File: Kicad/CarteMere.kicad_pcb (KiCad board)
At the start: 4 copper layers, 91 x 95 mm, 120 parts, among them J1 Conn_01x06, J10 Conn_01x04, J12 Conn_01x06, J13 Conn_01x06, J14 Conn_01x04, J15 Conn_01x04, J16 Conn_01x04, J18 Conn_01x06, J19 Conn_01x06, J2 Conn_01x10, J21 Conn_01x04, J22 Conn_01x04, J23 Conn_01x04, J24 Conn_01x02, J25 Conn_01x06, J26 Conn_01x02, J27 Conn_01x06, J28 Conn_01x06, J29 Conn_01x06, J3 Conn_01x10, J30 Conn_01x06, J31 Conn_01x02, J32 Conn_01x09, J33 Conn_01x05, J34 Conn_01x05, J35 Conn_01x05, J36 Conn_01x05, J37 Conn_01x05, J39 Conn_01x09, J4 Conn_01x10, J40 Conn_01x09, J41 Conn_01x05, J42 Conn_01x05, J43 Conn_01x05, J44 Conn_01x05, J45 Conn_01x05, J46 Conn_01x05, J47 Conn_01x05, J48 USB_C_Receptacle_USB2.0_16P, J49 Conn_01x02, J5 Conn_01x06, J50 Conn_ST_STDC14, J6 Conn_01x06, J7 Conn_01x06, J8 Conn_01x04, J9 Conn_01x04, SW1 SW_MEC_5E, U2 USBLC6-2P6, U3 STM32H573IITxQ

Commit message: ajout spi et maj readme
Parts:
- removed J15, J21, J23: Conn_01x04, Connector_PinHeader_2.54mm:PinHeader_1x04_P2.54mm_Vertical
- removed J24, J26, J31: Conn_01x02, Connector_PinHeader_2.54mm:PinHeader_1x02_P2.54mm_Vertical
- removed J4: Conn_01x10, Connector_PinHeader_2.54mm:PinHeader_1x10_P2.54mm_Vertical
- added J11: Conn_01x07, Connector_JST:JST_EH_B7B-EH-A_1x07_P2.50mm_Vertical, F.Cu at (161.5, 101.1)
- added J17: Conn_01x07, Connector_JST:JST_EH_B7B-EH-A_1x07_P2.50mm_Vertical, F.Cu at (167.7, 101.1)
- added R23: 51, Resistor_SMD:R_0402_1005Metric, B.Cu at (143.2, 78.5)
- J10: value Conn_01x04 -> Conn_01x05; footprint Connector_PinHeader_2.54mm:PinHeader_1x04_P2.54mm_Vertical -> Connector_JST:JST_EH_B5B-EH-A_1x05_P2.50mm_Vertical
- J16: value Conn_01x04 -> Conn_01x07; footprint Connector_PinHeader_2.54mm:PinHeader_1x04_P2.54mm_Vertical -> Connector_JST:JST_EH_B7B-EH-A_1x07_P2.50mm_Vertical
- J2, J3: value Conn_01x10 -> Conn_01x07; footprint Connector_PinHeader_2.54mm:PinHeader_1x10_P2.54mm_Vertical -> Connector_PinHeader_2.54mm:PinHeader_1x07_P2.54mm_Vertical
- J8: value Conn_01x04 -> Conn_01x07; footprint Connector_PinHeader_2.54mm:PinHeader_1x04_P2.54mm_Vertical -> Connector_PinHeader_2.54mm:PinHeader_1x07_P2.54mm_Vertical
- JP1: footprint TestPoint:TestPoint_2Pads_Pitch2.54mm_Drill0.8mm -> Connector_PinHeader_2.54mm:PinHeader_1x02_P2.54mm_Vertical
- SW1: footprint BoutonSMD:wurth_pushButton_SMD -> Switch:WS-TASU SMT Tact Switch 4.7x3.5 mm side push
- moved SW1 85.4 mm to (107.2, 142.7)
- moved J10 79.1 mm to (173.7, 89.3), turned to -90 degrees
- moved C6 77.0 mm to (108.9, 139.5), turned to 0 degrees
- moved J16 56.9 mm to (120.1, 78.8)
- moved J8 45.1 mm to (116.9, 103.8), turned to 180 degrees
- moved R14 17.7 mm to (157.6, 95.7)
- moved J37 6.97 mm to (105.1, 102.8)
- moved C34 6.50 mm to (160.9, 90.0)
- moved C35 6.50 mm to (160.9, 93.4)
- moved U4 6.50 mm to (164.8, 91.8)
- moved J34 5.79 mm to (105.1, 85.2)
- moved J2 4.76 mm to (114.4, 103.8)
- moved J3 4.76 mm to (111.8, 103.8)
- moved J42 4.61 mm to (104.1, 118.8)
- moved J44 4.10 mm to (104.1, 125.1)
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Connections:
- J10 pad 1: /TIM8_CH3 -> +3.3V
- J10 pad 2: /TIM8_CH2 -> GND
- J10 pad 3: /TIM8_CH1 -> /UART9_TX
- J10 pad 4: /TIM8_CH4 -> GND
- J16 pad 1: +3.3V -> /GPIO_PB11
- J16 pad 2: +3.3V -> /GPIO_PB10
- J16 pad 3: +3.3V -> /SPI5_SCK
- J16 pad 4: +3.3V -> /SPI5_MOSI
- J18 pad 1: /GPIO_PG0 -> /GPIO_PF14
- J18 pad 2: /GPIO_PG1 -> /GPIO_PF15
- J2 pad 1: /GPIO_PI9 -> +3.3V
- J2 pad 2: /GPIO_PI10 -> +3.3V
- J2 pad 3: /GPIO_PI11 -> +3.3V
- J2 pad 4: /GPIO_PG7 -> +3.3V
- J2 pad 5: /GPIO_PG6 -> +3.3V
- J2 pad 6: /GPIO_PG5 -> +3.3V
- J2 pad 7: /GPIO_PG4 -> +3.3V
- J3 pad 1: +3.3V -> GND
- J3 pad 2: +3.3V -> GND
- J3 pad 3: +3.3V -> GND
- J3 pad 4: +3.3V -> GND
- J3 pad 5: +3.3V -> GND
- J3 pad 6: +3.3V -> GND
- J3 pad 7: +3.3V -> GND
- J8 pad 1: /TIM3_CH4 -> /GPIO_PG7
- J8 pad 2: /TIM3_CH1 -> /GPIO_PG6
- J8 pad 3: /TIM3_CH3 -> /GPIO_PG5
- J8 pad 4: /TIM3_CH2 -> /GPIO_PG4
- R14 pad 1: Net-(U3-PA6) -> Net-(U3-PF3)
- U3 pad 10: /MCU/Osc_OUT -> unconnected-(U3-PC15-Pad10)
- U3 pad 11: /GPIO_PI9 -> unconnected-(U3-PI9-Pad11)
- U3 pad 115: /TIM3_CH1 -> unconnected-(U3-PC6-Pad115)
- U3 pad 116: /TIM8_CH2 -> unconnected-(U3-PC7-Pad116)
- U3 pad 117: /TIM3_CH3 -> unconnected-(U3-PC8-Pad117)
- U3 pad 12: /GPIO_PI10 -> unconnected-(U3-PI10-Pad12)
- U3 pad 13: /GPIO_PI11 -> unconnected-(U3-PI11-Pad13)
- U3 pad 163: /TIM3_CH2 -> unconnected-(U3-PB5-Pad163)
- U3 pad 174: /TIM8_CH1 -> unconnected-(U3-PI5-Pad174)
- U3 pad 19: unconnected-(U3-PF3-Pad19) -> Net-(U3-PF3)
- U3 pad 20: unconnected-(U3-PF4-Pad20) -> /USART11_RX
- U3 pad 26: unconnected-(U3-PF8-Pad26) -> /SPI5_MISO
- U3 pad 27: unconnected-(U3-PF9-Pad27) -> /SPI5_MOSI
- U3 pad 28: unconnected-(U3-PH0-Pad28) -> /MCU/Osc_IN
- U3 pad 29: unconnected-(U3-PH1-Pad29) -> /MCU/Osc_OUT
- U3 pad 4: unconnected-(U3-PE5-Pad4) -> /SPI4_MISO
- U3 pad 42: unconnected-(U3-PH2-Pad42) -> /GPIO_PH2
- U3 pad 43: unconnected-(U3-PH3-Pad43) -> /GPIO_PH3
- U3 pad 48: unconnected-(U3-PA5-Pad48) -> /SPI6_SCK
- U3 pad 49: Net-(U3-PA6) -> /SPI6_MISO
- U3 pad 5: unconnected-(U3-PE6-Pad5) -> /SPI4_MOSI
- U3 pad 50: /USART11_RX -> /SPI6_MOSI
- U3 pad 54: /TIM3_CH4 -> unconnected-(U3-PB1-Pad54)
- U3 pad 60: /ADC2_INP2 -> unconnected-(U3-PF13-Pad60)
- U3 pad 61: /ADC2_INP6 -> /GPIO_PF14
- U3 pad 62: unconnected-(U3-PF15-Pad62) -> /GPIO_PF15
- U3 pad 63: /GPIO_PG0 -> /UART9_RX
- U3 pad 64: /GPIO_PG1 -> Net-(U3-PG1)
- U3 pad 7: /TIM8_CH4 -> /GPIO_PI8
- U3 pad 72: unconnected-(U3-PE12-Pad72) -> /SPI4_SCK
- U3 pad 76: unconnected-(U3-PB10-Pad76) -> /GPIO_PB10
- U3 pad 77: unconnected-(U3-PB11-Pad77) -> /GPIO_PB11
- U3 pad 8: unconnected-(U3-PC13-Pad8) -> /GPIO_PC13
- U3 pad 84: unconnected-(U3-PH6-Pad84) -> /SPI5_SCK
- U3 pad 87: /TIM8_CH3 -> unconnected-(U3-PH10-Pad87)
- U3 pad 9: /MCU/Osc_IN -> unconnected-(U3-PC14-Pad9)
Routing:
- net /TIM8_CH4: track 87.6 -> 0.00 mm, vias 1 -> 0
- net /TIM8_CH1: track 77.7 -> 0.00 mm, vias 1 -> 0
- net /TIM8_CH3: track 77.5 -> 0.00 mm, vias 3 -> 0
- net /GPIO_PG0: track 62.5 -> 0.00 mm, vias 1 -> 0
- net /SPI5_MISO: track 0.00 -> 60.1 mm, vias 0 -> 2
- net /SPI5_MOSI: track 0.00 -> 60.1 mm, vias 0 -> 2
- net /TIM8_CH2: track 60.0 -> 0.00 mm, vias 1 -> 0
- net /GPIO_PF14: track 0.00 -> 59.6 mm, vias 0 -> 1
- net /GPIO_PG1: track 58.6 -> 0.00 mm, vias 1 -> 0
- net /GPIO_PF15: track 0.00 -> 57.5 mm, vias 0 -> 1
- net /UART9_RX: track 0.00 -> 50.4 mm, vias 0 -> 2
- net /UART9_TX: track 0.00 -> 47.1 mm, vias 0 -> 1
- net /SPI6_MISO: track 0.00 -> 45.3 mm, vias 0 -> 1
- net /SPI4_SCK: track 0.00 -> 43.7 mm, vias 0 -> 2
- net /SPI6_MOSI: track 0.00 -> 43.3 mm, vias 0 -> 1
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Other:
- board text added: "MISO"
- board text added: "MOSI"
- board text added: "PB10"
- board text added: "PB11"
- board text added: "PC13"
- board text added: "PH2"
- board text added: "PH3"
- board text added: "PI8"
- board text added: "SCK"
- board text added: "SPI4"
- board text added: "SPI5"
- board text added: "SPI6"
- board text added: "UART9"
- board text removed: "PI10"
- board text removed: "PI11"
- board text removed: "PI9"
- board text removed: "TIM3"
- board text removed: "TIMER8"
- board text removed: "UART12"

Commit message: final push--ajout des vias
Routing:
- net GND: vias 379 -> 472

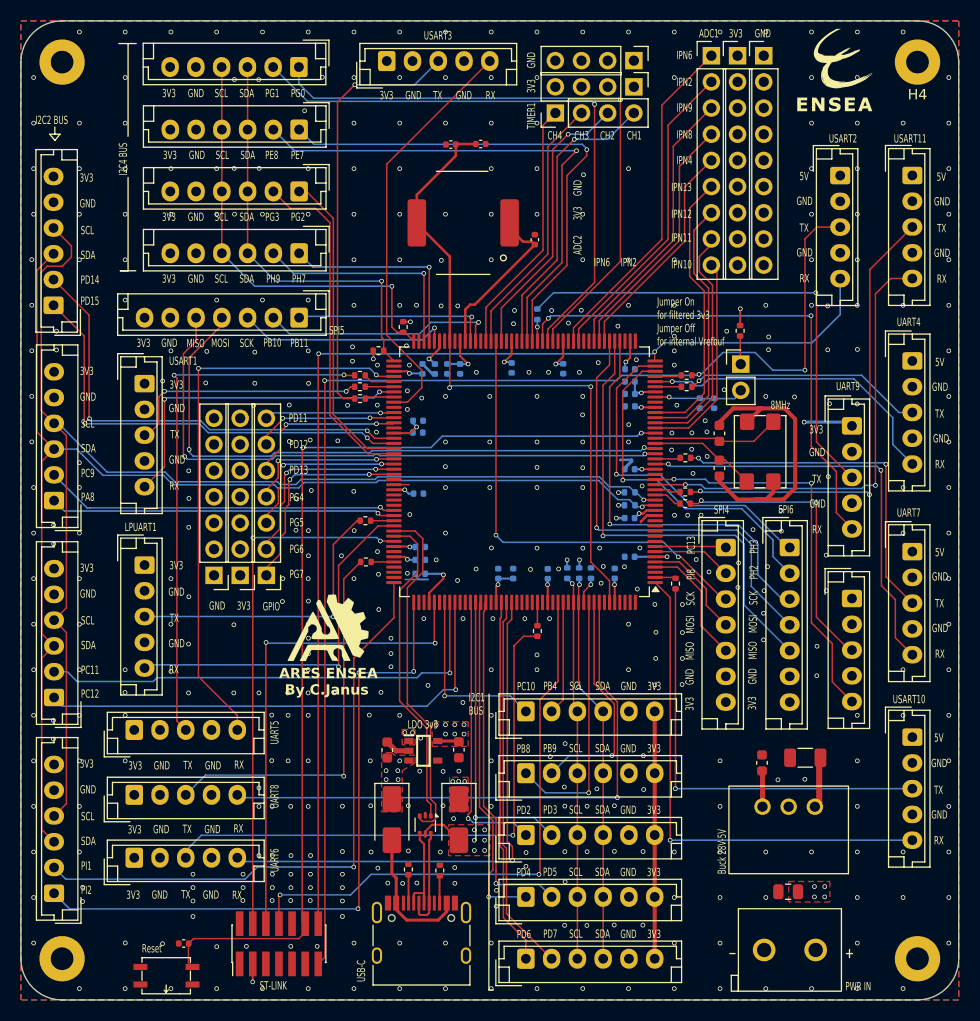
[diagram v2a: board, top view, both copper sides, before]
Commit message: ajout d'un connecteur SPI
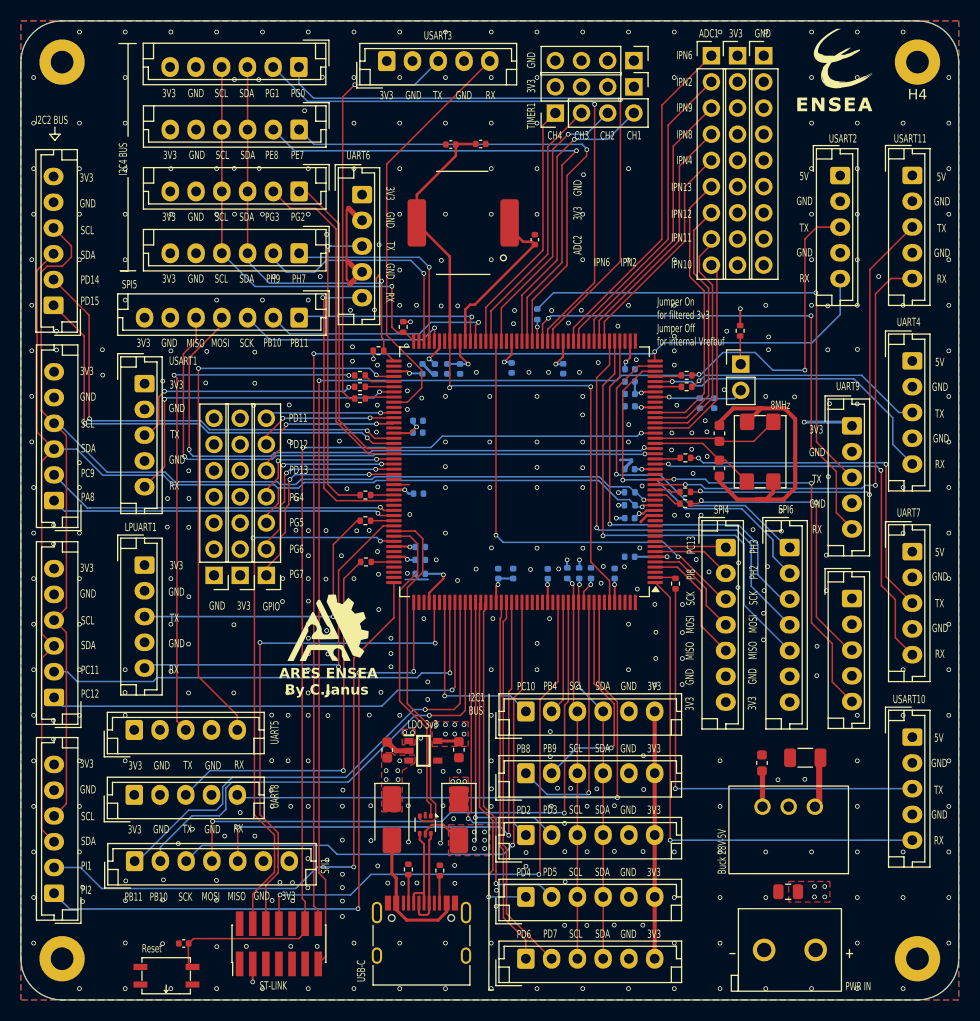
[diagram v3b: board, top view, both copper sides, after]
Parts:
- removed R10: 51, Resistor_SMD:R_0402_1005Metric
- added J4: Conn_01x07, Connector_JST:JST_EH_B7B-EH-A_1x07_P2.50mm_Vertical, F.Cu at (104.1, 131.5)
- added R24: 51, Resistor_SMD:R_0402_1005Metric, F.Cu at (126.5, 96.0)
- moved J47 68.0 mm to (126.2, 66.9), turned to -90 degrees
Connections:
- U3 pad 115: unconnected-(U3-PC6-Pad115) -> Net-(U3-PC6)
- U3 pad 116: unconnected-(U3-PC7-Pad116) -> /USART6_RX
- U3 pad 142: unconnected-(U3-PD0-Pad142) -> /GPIO_PD0
- U3 pad 143: unconnected-(U3-PD1-Pad143) -> /GPIO_PD1
- U3 pad 152: /USART6_RX -> /SPI1_MISO
- U3 pad 154: unconnected-(U3-PG11-Pad154) -> /SPI1_SCK
- U3 pad 157: Net-(U3-PG14) -> unconnected-(U3-PG14-Pad157)
- U3 pad 163: unconnected-(U3-PB5-Pad163) -> /SPI1_MOSI
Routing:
- net /SPI1_MOSI: track 0.00 -> 59.0 mm, vias 0 -> 2
- net /SPI1_SCK: track 0.00 -> 57.0 mm, vias 0 -> 1
- net /SPI1_MISO: track 0.00 -> 52.7 mm, vias 0 -> 2
- net /GPIO_PD0: track 0.00 -> 48.7 mm, vias 0 -> 1
- net /GPIO_PD1: track 0.00 -> 48.1 mm, vias 0 -> 1
- net /USART6_TX: track 54.1 -> 30.0 mm
- net /USART6_RX: track 52.3 -> 29.7 mm
- net GND: track 43.9 -> 57.2 mm, vias 472 -> 480
- net Net-(U3-PG14): track 2.27 -> 0.00 mm
- net Net-(U3-PC6): track 0.00 -> 2.26 mm
- net /MCU/SWCLK: track 47.7 -> 49.5 mm
- net /MCU/SWDIO: track 51.3 -> 53.0 mm
- net /GPIO_PH9: track 22.0 -> 23.3 mm
- net /USART2_TX: track 122.5 -> 123.4 mm
- net /USART3_TX: track 41.5 -> 40.8 mm
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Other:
- board text added: "SPI1"
